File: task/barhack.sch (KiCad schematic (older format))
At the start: 85 parts, among them IC1 SIM900, J1 dc_jack, J10 SWD, J2 SIMHOLDER, J3 U.FL, J4 IO, J5 BOOT0, J6 BOOT0, J7 EX1, J8 ACCEPTOR, J9 EX2, Q1 NPN_BEC, Q2 NPN_BEC, Q3 BSS138, Q4 BSS138, Q5 NPN_BEC, Q6 NPN_BEC, Q7 NPN_BEC, SW1 BBPWR, SW2 BBPWR, U1 MIC29302, U2 LM1117-SOT, U3 STM32F103C8, X1 8M

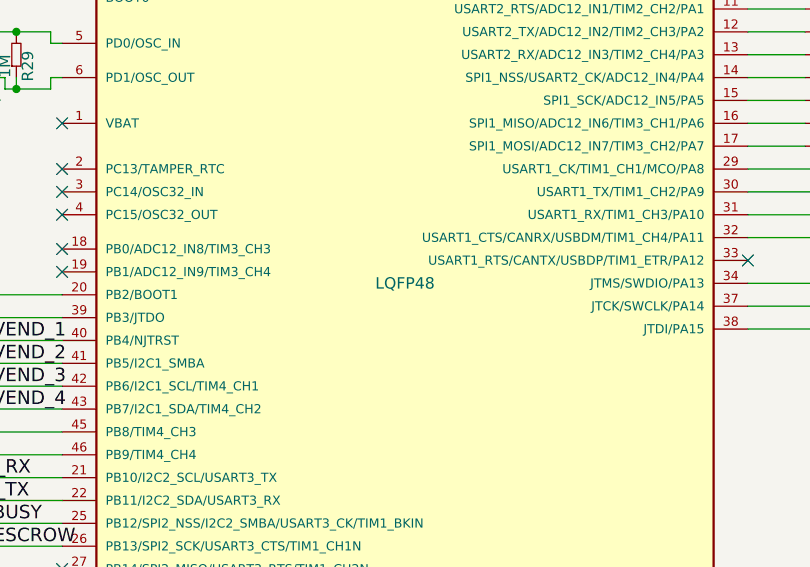
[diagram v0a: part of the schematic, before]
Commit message: Remove footprint of U3 from schematic.
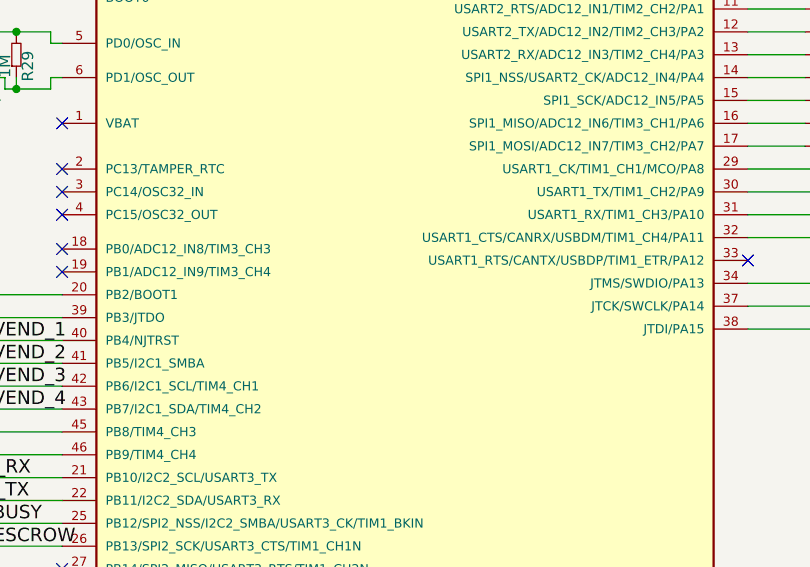
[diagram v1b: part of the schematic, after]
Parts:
- U3: footprint LQFP48 -> (none)
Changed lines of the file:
@@
 F 0 "U3" H 10250 8650 50  0000 C CNN
 F 1 "STM32F103C8" H 12600 5350 50  0000 C CNN
-F 2 "LQFP48" H 11550 7000 50  0000 C CNN
+F 2 "" H 11550 7000 50  0000 C CNN
 F 3 "" H 11550 7000 60  0000 C CNN
 	1    11550 7000

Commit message: Fiiiiinal design for CONFidence, sent off to fab house.
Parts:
- added C21, C22, C23: 100n, w_smd_cap:c_0603, symbol C
- C1, C4, C5: footprint (none) -> w_smd_cap:c_elec_8x10
- C10, C11, C12, C13, C14, C15, C16, C17, C3, C6, C7, C8, C9: footprint (none) -> w_smd_cap:c_0603
- C2: footprint (none) -> w_smd_cap:c_tant_C
- F1: footprint (none) -> w_misc_comp:fuse_holder_CQ-2
- IC1: footprint (none) -> sim900:SIM900
- J1: value dc_jack -> 5V DC; footprint (none) -> w_conn_misc:dc_socket
- J10: footprint (none) -> w_pin_strip:pin_strip_5x2
- J2: footprint (none) -> sim900:C707-10M006-049-2
- J3: footprint (none) -> w_conn_rf:coaxial_u.fl-r-smt-1; symbol HEADER_4 -> HEADER_3
- J4: footprint (none) -> w_conn_screw:mstbva_2,5%2f9-g-5,08
- J5, J6: footprint (none) -> w_pin_strip:pin_strip_3
- J7: footprint (none) -> w_pin_strip:pin_strip_4x2
- J8: footprint (none) -> w_pin_strip:pin_strip_8x2
- J9: footprint (none) -> w_pin_strip:pin_strip_2x2
- LD1, LD2, LD3, LD4, LD5, LD6, LD7: footprint (none) -> w_smd_leds:Led_0603
- Q1, Q2, Q3, Q4, Q5, Q6, Q7: footprint (none) -> w_smd_trans:sot23
- R1, R10, R11, R12, R13, R14, R15, R16, R17, R18, R19, R2, R20, R21, R22, R23, R24, R25, R26, R27, R28, R29, R3, R30, R31, R32, R33, R34, R35, R36, R4, R5, R6, R7, R8, R9: footprint (none) -> w_smd_resistors:r_0603
- SW1: footprint (none) -> w_switch:smd_push
- SW2: value BBPWR -> APP_RESET; footprint (none) -> w_switch:smd_push
- U1: footprint (none) -> w_smd_trans:d-pak-5
- U2: footprint (none) -> w_smd_trans:d-pak
- U3: footprint (none) -> w_smd_lqfp:lqfp48
- X1: footprint (none) -> w_crystal:hc-49_smd
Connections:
- net +BATT: now also C21.1, C22.1, C23.1
- net GND: now also C21.2, C22.2, C23.2; no longer J3.4, J8.4, J8.9, R32.1, R36.1, U3.25 (PB12/SPI2_NSS/I2C2_SMBA/USART3_CK/TIM1_BKIN), U3.43 (PB7/I2C1_SDA/TIM4_CH2)
- net at U3.29 (USART1_CK/TIM1_CH1/MCO/PA8): now also J9.4; no longer J9.1
- net at U3.30 (USART1_TX/TIM1_CH2/PA9): now also J9.3; no longer J9.2
- net at U3.31 (USART1_RX/TIM1_CH3/PA10): now also J9.2; no longer J9.3
- net at U3.32 (USART1_CTS/CANRX/USBDM/TIM1_CH4/PA11): now also J9.1; no longer J9.4
- new net A_BUSY: J8.9, R36.1, U3.25 (PB12/SPI2_NSS/I2C2_SMBA/USART3_CK/TIM1_BKIN)
- new net A_VEND_4: J8.4, R32.1, U3.43 (PB7/I2C1_SDA/TIM4_CH2)
